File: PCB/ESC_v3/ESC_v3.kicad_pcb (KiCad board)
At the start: 4 copper layers, 42 x 83.5 mm, 130 parts, among them J1 Conn_01x04_Pin, J10 Conn_01x01_Pin, J11 Screw_Terminal_01x01, J2 Screw_Terminal_01x01, J3 Conn_01x01_Pin, J4 Conn_01x01_Pin, J5 Conn_01x01_Pin, J6 Conn_01x01_Pin, J7 Conn_01x01_Pin, J8 Conn_01x01_Pin, J9 Conn_01x01_Pin, Q1 NTMFS2D1N08XT1G, Q2 NTMFS2D1N08XT1G, Q3 NTMFS2D1N08XT1G, Q4 NTMFS2D1N08XT1G, Q5 NTMFS2D1N08XT1G, Q6 NTMFS2D1N08XT1G, U1 SN65HVD232, U2 DRV8323SRTAT, U5 STM32G431CBTx, Y2 16MHz

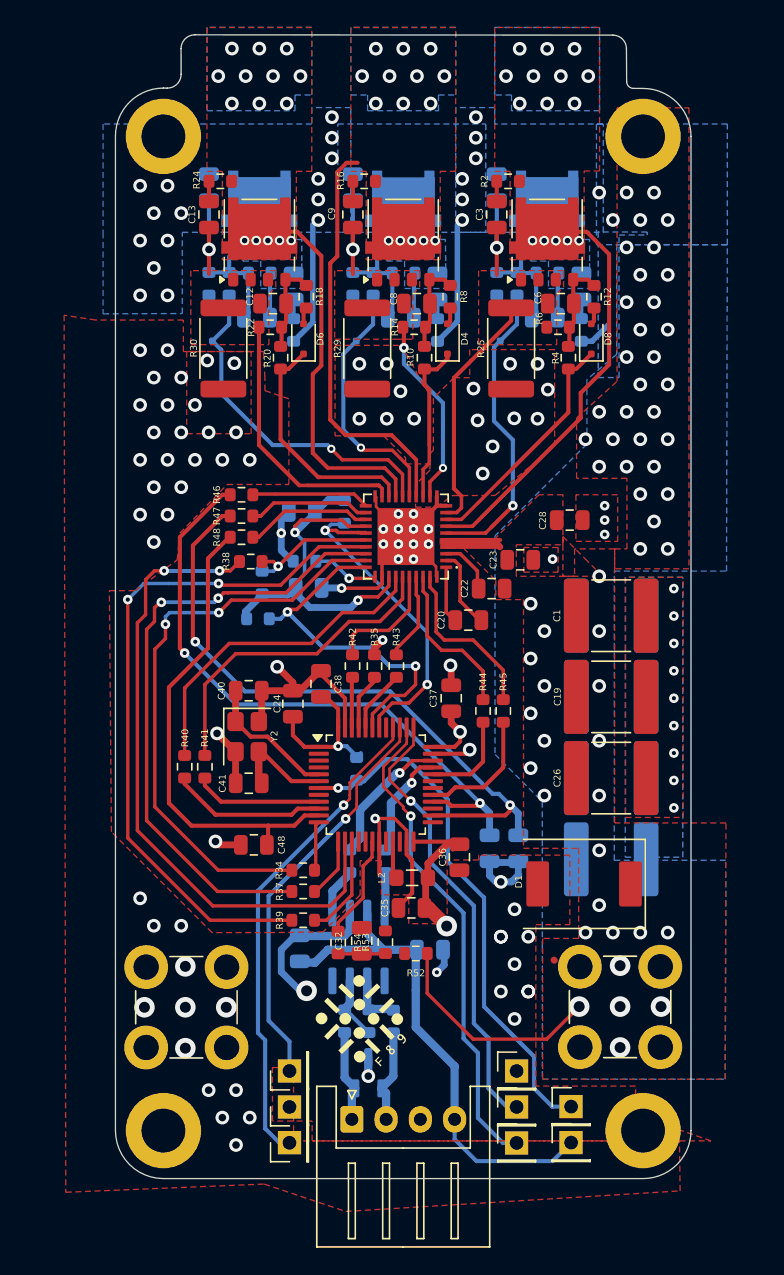
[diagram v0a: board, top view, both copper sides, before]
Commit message: Update ESC_v3 PCB layout and backup files
Removed old backup ZIPs and added new ones for ESC_v3. Modified ESC_v3.kicad_pcb: added several unnamed footprints, a test point, and adjusted component placements. Made significant changes to net routing, via placements, and segment connections, especially around the power and ground nets. Updated some net segment widths and reorganized connections for improved layout and clarity.
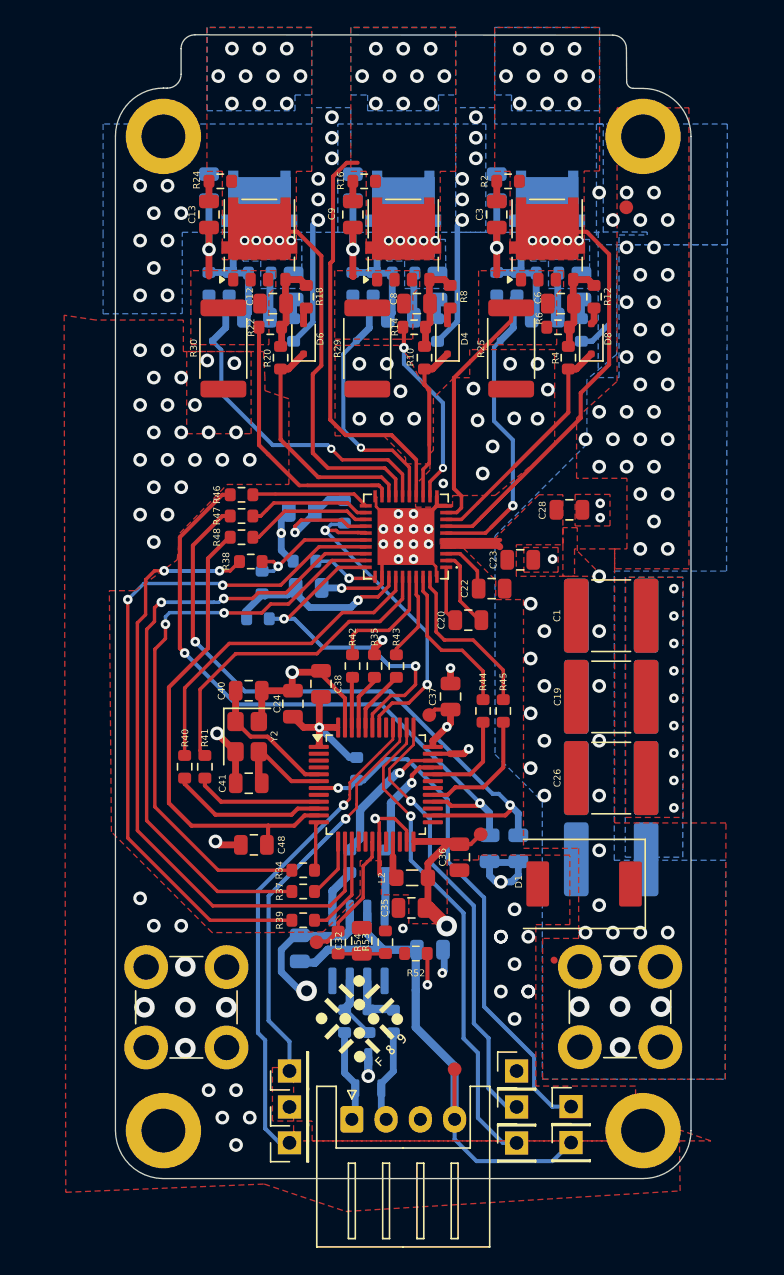
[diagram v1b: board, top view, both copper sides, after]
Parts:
- added ?: , , F.Cu at (148.9, 105.5)
- added ?: , , F.Cu at (150.8, 88.3)
- added ?: , , F.Cu at (138.9, 96.2)
- added ?: , , F.Cu at (147.1, 79.6)
- added REF**: TestPoint_Pad_D1.0mm, TestPoint:TestPoint_Pad_D1.0mm, F.Cu at (161.5, 42.6)
- moved C28 0.75 mm to (157.3, 64.7)
- moved C37 0.13 mm to (148.7, 78.3)
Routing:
- net 3V3: track 151.6 -> 161.9 mm
- net GND: track 87.1 -> 79.9 mm, vias 98 -> 99
- net SPA: track 24.7 -> 28.2 mm
- net V_BAT_MEAS: track 7.57 -> 9.43 mm
- net Net-(D8-A): track 1.23 -> 2.18 mm
- net G_A_L: track 17.5 -> 18.0 mm
- net V_BAT: track 49.9 -> 49.4 mm, vias 78 -> 79
- added copper zone on In2.Cu, net GND

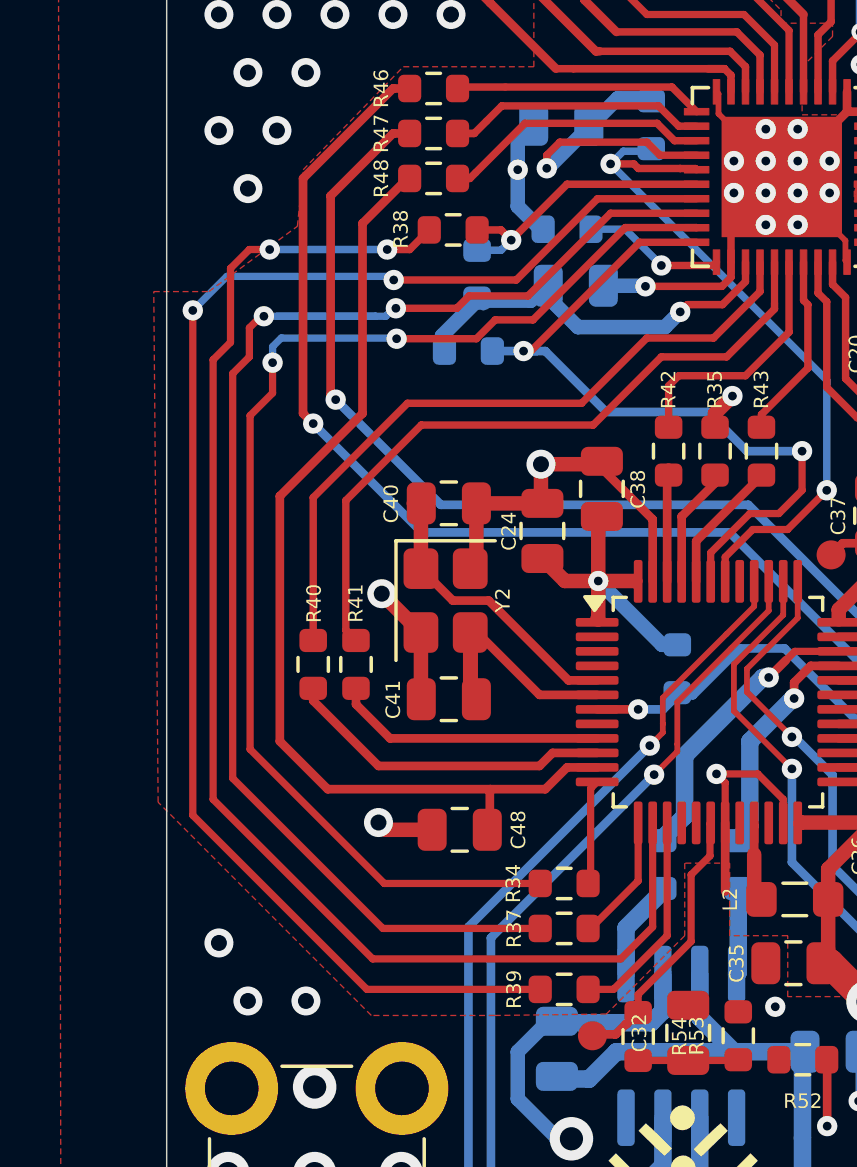
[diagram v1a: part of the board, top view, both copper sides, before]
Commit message: Update ESC_v3 PCB layout and routing
Adjusted footprints and positions for several components (crystals, resistors, capacitors) on the ESC_v3 PCB. Updated net routing and via placements, especially around the oscillator and decoupling capacitor areas. Improved net connections for nets 1, 15, 20, 21, 25, and 53, optimizing signal paths and component placement. Replaced an old backup with a new one.
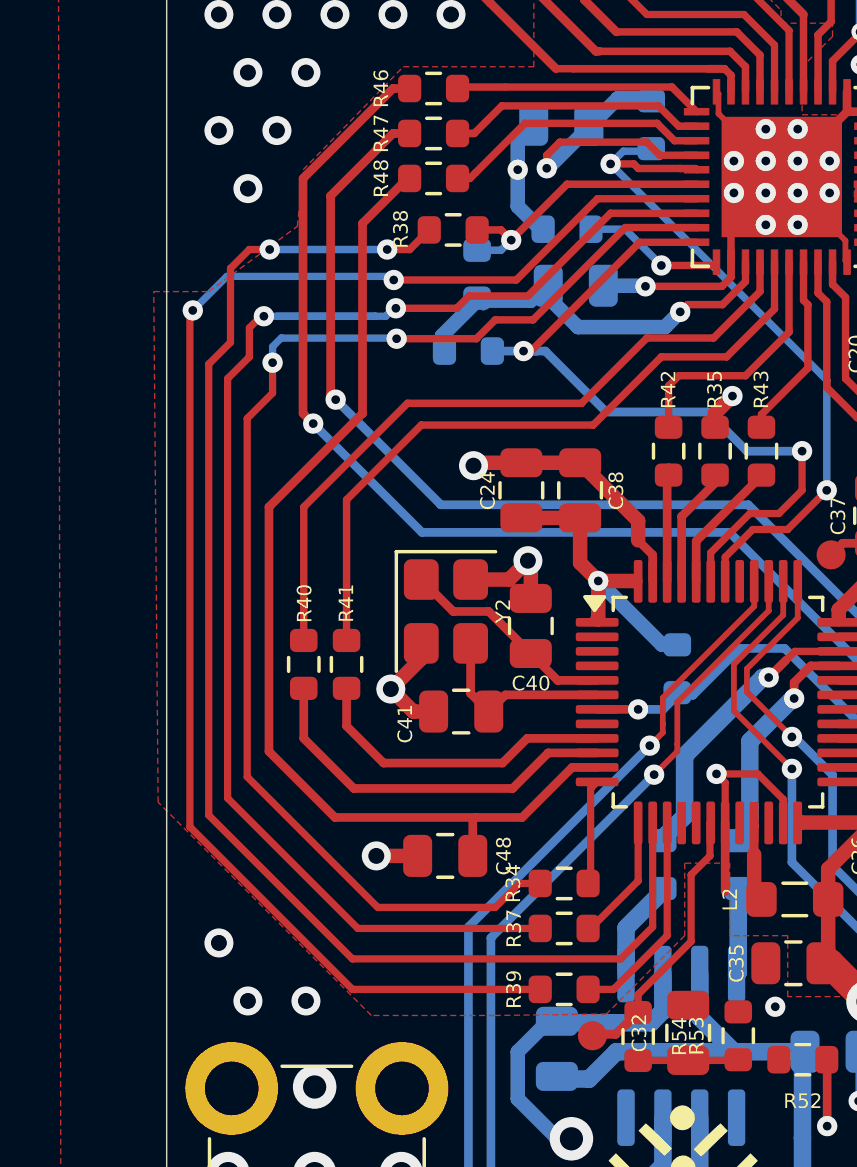
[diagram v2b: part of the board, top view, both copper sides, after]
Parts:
- moved C40 5.08 mm to (136.8, 82.1), turned to 90 degrees
- moved C24 1.58 mm to (136.4, 77.4)
- moved C48 1.03 mm to (133.8, 90.0)
- moved C38 0.75 mm to (138.4, 77.4)
- moved C41 0.60 mm to (134.3, 85.0)
- moved Y2 0.38 mm to (133.8, 81.6)
- moved R40 0.32 mm to (128.9, 83.4)
- moved R41 0.32 mm to (130.4, 83.4)
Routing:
- net /MCU/OSC_OUT: track 10.1 -> 6.58 mm
- net /MCU/OSC_IN: track 10.4 -> 7.50 mm
- net GND: track 79.9 -> 77.8 mm, vias 99 -> 100
- net /MCU/TIM15_CH1: track 11.3 -> 13.1 mm
- net /MCU/ADC1_IN4: track 34.6 -> 36.1 mm
- net /MCU/TIM15_CH1N: track 9.35 -> 10.8 mm
- net nSCS: track 42.4 -> 43.7 mm
- net SCLK: track 48.9 -> 49.5 mm
- net /MCU/SPI1_MISO: track 51.3 -> 51.8 mm

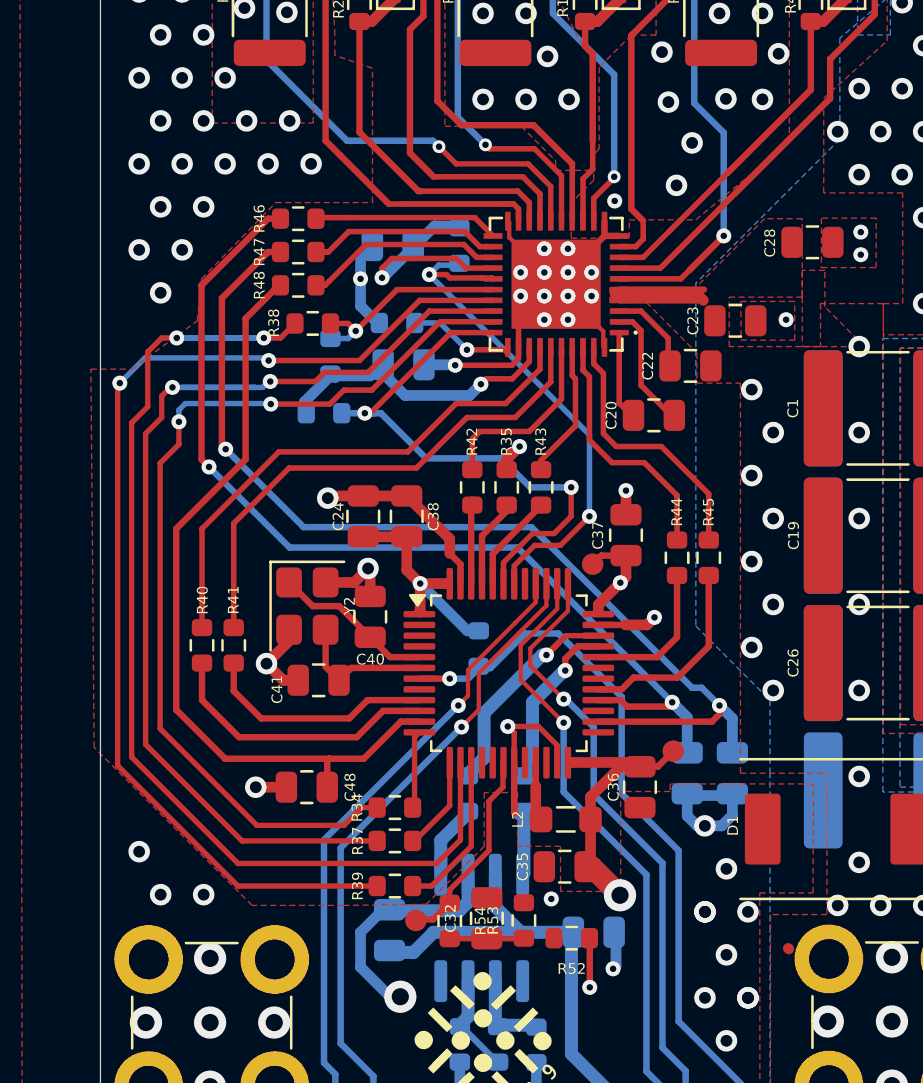
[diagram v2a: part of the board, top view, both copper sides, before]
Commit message: Update ESC_v3 PCB routing and backups
Remove older ESC_v3 backup ZIPs and add new timestamped backups, and apply routing edits to ESC_v3.kicad_pcb. Changes include moved/adjusted track segments and vias, updated track widths and coordinates, and refreshed UUIDs for many nets; ESC_v3.kicad_prl was also modified. These edits reflect PCB routing cleanup/rework and repository backup housekeeping.
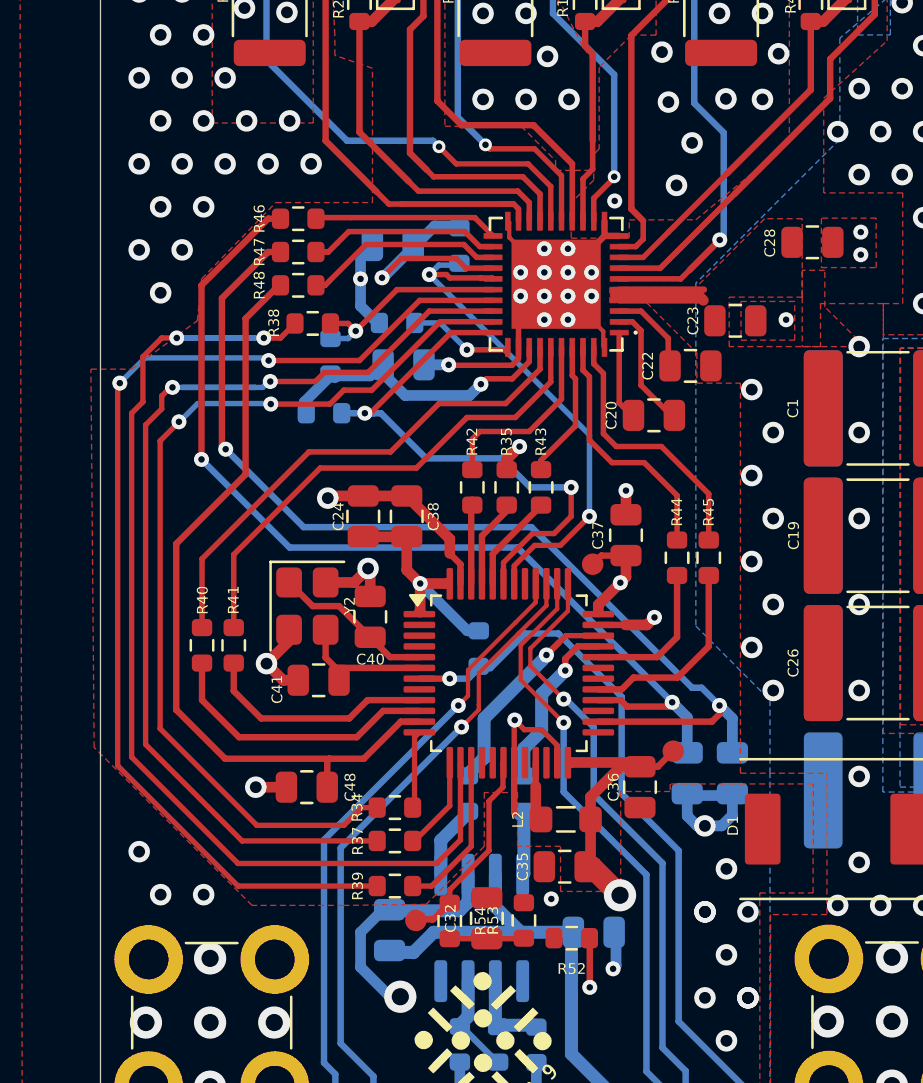
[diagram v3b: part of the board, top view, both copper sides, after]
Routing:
- net INLA: track 23.9 -> 23.1 mm
- net INHA: track 24.4 -> 23.6 mm
- net /MCU/OSC_OUT: track 6.58 -> 5.86 mm

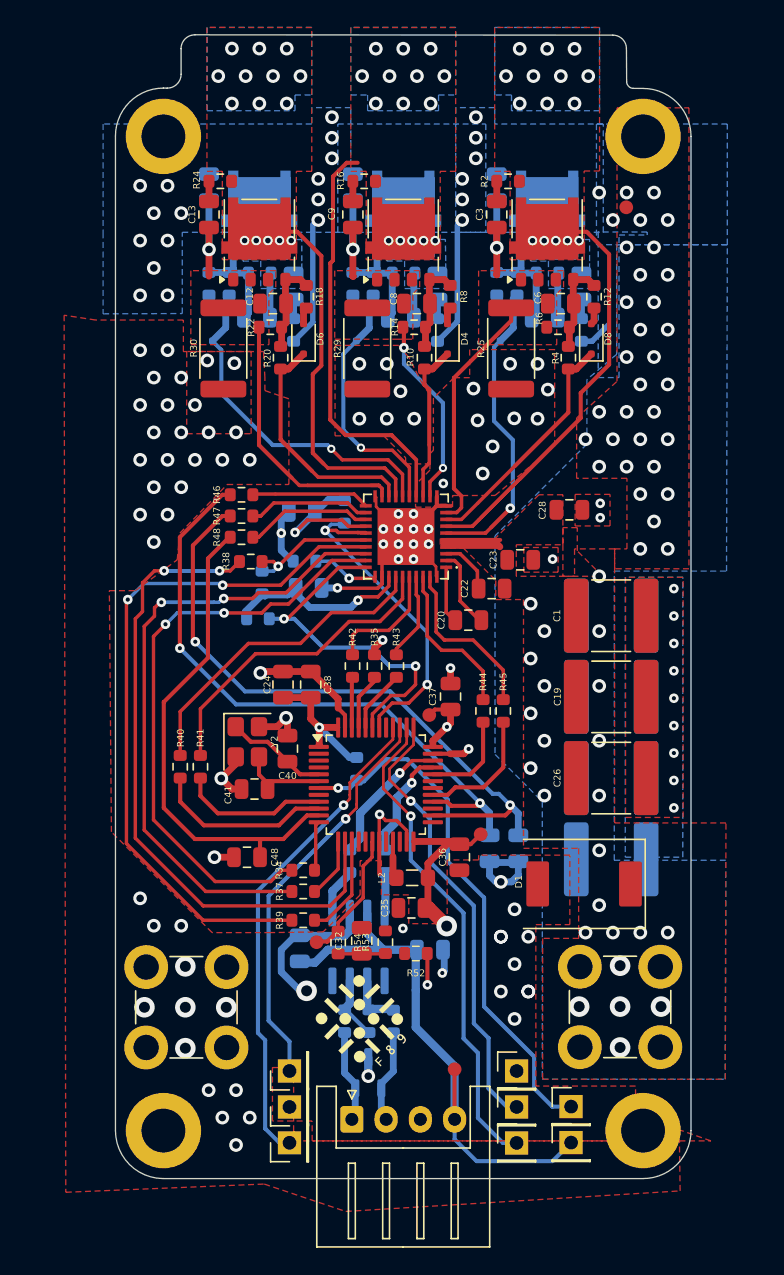
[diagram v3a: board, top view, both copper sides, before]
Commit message: Fix DRVR schematic wiring and PCB nets
Clean up DRVR.kicad_sch by adding/removing junctions and wires, rerouting traces and repositioning symbols; update component properties (capacitor values/ratings and label positions). Update ESC_v3.kicad_pcb to match schematic changes: reorder/renumber nets, correct pin/net assignments and adjust footprints/placements. Remove many outdated ESC_v3-backups ZIPs and add new timestamped backup ZIPs; add STM/STM.ioc and update MCU.kicad_sch and related project files. These changes correct net mappings and tidy schematic/PCB routing and metadata.
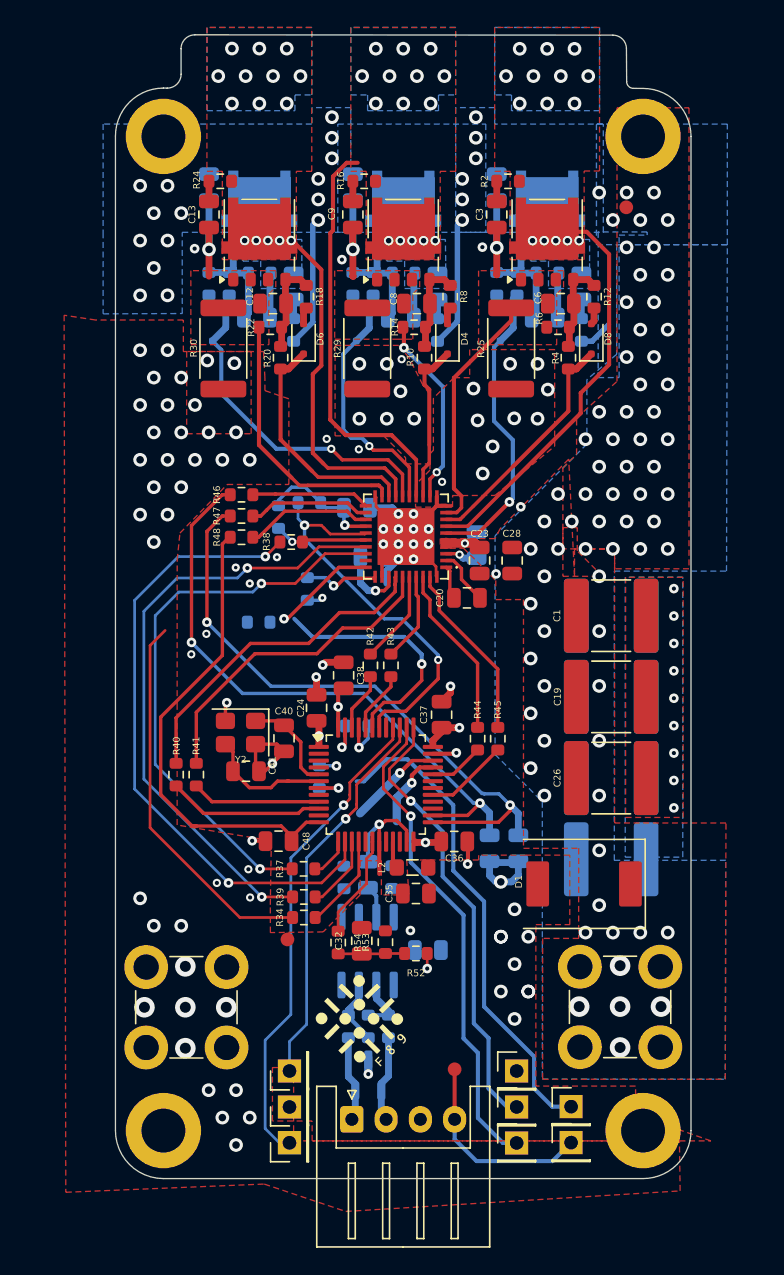
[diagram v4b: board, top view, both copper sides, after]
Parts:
- removed the ? at (150.8, 88.3)
- removed the ? at (147.1, 79.6)
- C20: value 47nF -> 47n/VM-rated
- C21: value 1uF -> 1u/6.3V
- C22: value 1uF -> 1u/16V; moved to B.Cu
- C23: value 0.1uF -> 100n
- C25: value 47nF -> 100n/6.3V
- R35: moved to B.Cu
- U5: value STM32G431CBTx -> STM32G431CBT6
- moved C17 9.35 mm to (147.0, 96.8), turned to 0 degrees
- moved C16 7.10 mm to (142.6, 91.3), turned to 90 degrees
- moved C28 5.58 mm to (153.2, 68.3), turned to -90 degrees
- moved C21 5.24 mm to (143.0, 68.1)
- moved R28 4.92 mm to (136.1, 65.2), turned to 90 degrees
- moved R35 4.56 mm to (141.8, 80.4), turned to 180 degrees
- moved C25 4.04 mm to (141.8, 64.5)
- moved R34 3.45 mm to (137.9, 94.4)
- moved C22 3.36 mm to (150.6, 67.2), turned to -90 degrees
- moved R38 3.28 mm to (137.0, 67.0)
- moved C24 2.98 mm to (138.9, 79.1)
- moved C23 2.96 mm to (150.8, 68.3), turned to -90 degrees
- moved R36 2.79 mm to (139.1, 84.2)
- moved R27 2.64 mm to (138.3, 64.1), turned to 0 degrees
- moved C48 2.58 mm to (136.1, 88.8)
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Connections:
- C25 pad 1: GND -> 3V3
- C25 pad 2: 3V3 -> GND
- C46 pad 1: /MCU/ADC1_IN5 -> /MCU/ADC1_IN11
- C47 pad 1: /MCU/ADC1_IN11 -> /MCU/ADC1_IN14
- C48 pad 1: /MCU/ADC1_IN4 -> /MCU/ADC2_IN12
- R46 pad 1: /MCU/ADC1_IN5 -> /MCU/ADC1_IN11
- R47 pad 1: /MCU/ADC1_IN11 -> /MCU/ADC1_IN14
- R48 pad 1: /MCU/ADC1_IN4 -> /MCU/ADC2_IN12
- U5 pad 11: /MCU/ADC1_IN4 -> unconnected-(U5-PA3-Pad11)
- U5 pad 12: /MCU/SPI1_NSS/CS -> /MCU/ADC2_IN12
- U5 pad 16: unconnected-(U5-PB0-Pad16) -> /MCU/SPI1_NSS/CS
- U5 pad 25: unconnected-(U5-PB11-Pad25) -> /MCU/ADC1_IN14
- U5 pad 28: /MCU/ADC1_IN5 -> unconnected-(U5-PB14-Pad28)
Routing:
- net 3V3: track 161.5 -> 102.7 mm, vias 5 -> 7
- net /MCU/ADC1_IN5: track 46.0 -> 0.00 mm, vias 2 -> 0
- net /MCU/ADC1_IN14: track 0.00 -> 45.2 mm, vias 0 -> 2
- net /MCU/ADC1_IN4: track 36.1 -> 0.00 mm
- net /MCU/ADC2_IN12: track 0.00 -> 34.9 mm
- net GND: track 77.7 -> 61.1 mm, vias 100 -> 112
- net nSCS: track 43.4 -> 28.0 mm, vias 2 -> 0
- net SCLK: track 49.5 -> 41.2 mm
- net SDI: track 51.2 -> 44.8 mm
- net /MCU/SPI1_MISO: track 51.8 -> 46.3 mm
- net V_A_PHASE: track 39.3 -> 34.2 mm
- net NFAULT: track 24.3 -> 28.8 mm
- net V_BAT: track 49.4 -> 45.3 mm, vias 79 -> 92
- net /MCU/OSC_OUT: track 5.86 -> 9.58 mm
- net Net-(U1-D): track 3.39 -> 0.00 mm
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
